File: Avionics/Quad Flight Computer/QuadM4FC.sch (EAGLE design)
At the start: 1 part, among them U1 INF-PG-LQFP-100-11-7000X7000E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

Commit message: Added avionics library as Eagle-Library submodule.
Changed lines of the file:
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@@
+</nets>
+</sheet>
+<sheet>
+<description>Sensors</description>
+<plain>
+</plain>
+<instances>
+</instances>
+<busses>
+</busses>
+<nets>
+</nets>
+</sheet>
+<sheet>
+<description>2.4 GHz Radio</description>
+<plain>
+</plain>
+<instances>
+</instances>
+<busses>
+</busses>
+<nets>
+</nets>
+</sheet>
+<sheet>
+<description>900MHz Radio</description>
+<plain>
+</plain>
+<instances>
+</instances>
+<busses>
+</busses>
+<nets>
+</nets>
+</sheet>
+<sheet>
+<description>Flash Memory</description>
+<plain>
+</plain>
+<instances>
+</instances>
+<busses>
+</busses>
+<nets>
+</nets>
+</sheet>
+<sheet>
+<description>Power</description>
+<plain>
+</plain>
+<instances>
+</instances>
+<busses>
+</busses>
+<nets>
+</nets>
+</sheet>
+<sheet>
+<description>Connectors</description>
+<plain>
+</plain>
+<instances>
+</instances>
+<busses>
+</busses>
+<nets>
 </nets>
 </sheet>

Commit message: Added IMU to library
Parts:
- added U2: MPU-9250, Invesense:MPU-9250
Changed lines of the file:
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@@
 <layers>
 <layer number="1" name="Top" color="4" fill="1" visible="no" active="no"/>
+<layer number="2" name="Route2" color="1" fill="3" visible="no" active="no"/>
+<layer number="3" name="Route3" color="4" fill="3" visible="no" active="no"/>
+<layer number="14" name="Route14" color="1" fill="6" visible="no" active="no"/>
+<layer number="15" name="Route15" color="4" fill="6" visible="no" active="no"/>
 <layer number="16" name="Bottom" color="1" fill="1" visible="no" active="no"/>
 <layer number="17" name="Pads" color="2" fill="1" visible="no" active="no"/>
@@
 <layer number="48" name="Document" color="7" fill="1" visible="no" active="no"/>
 <layer number="49" name="Reference" color="7" fill="1" visible="no" active="no"/>
+<layer number="50" name="dxf" color="7" fill="1" visible="no" active="no"/>
 <layer number="51" name="tDocu" color="7" fill="1" visible="no" active="no"/>
 <layer number="52" name="bDocu" color="7" fill="1" visible="no" active="no"/>
+<layer number="53" name="tGND_GNDA" color="7" fill="1" visible="no" active="no"/>
+<layer number="54" name="bGND_GNDA" color="7" fill="1" visible="no" active="no"/>
+<layer number="56" name="wert" color="7" fill="1" visible="no" active="no"/>
 <layer number="91" name="Nets" color="2" fill="1" visible="yes" active="yes"/>
 <layer number="92" name="Busses" color="1" fill="1" visible="yes" active="yes"/>
@@
 <layer number="97" name="Info" color="7" fill="1" visible="yes" active="yes"/>
 <layer number="98" name="Guide" color="6" fill="1" visible="yes" active="yes"/>
+<layer number="100" name="Muster" color="7" fill="1" visible="yes" active="yes"/>
+<layer number="101" name="Patch_Top" color="7" fill="1" visible="yes" active="yes"/>
+<layer number="102" name="Vscore" color="7" fill="1" visible="yes" active="yes"/>
+<layer number="103" name="tMap" color="7" fill="1" visible="yes" active="yes"/>
+<layer number="104" name="Name" color="7" fill="1" visible="yes" active="yes"/>
+<layer number="105" name="tPlate" color="7" fill="1" visible="yes" active="yes"/>
+<layer number="106" name="bPlate" color="7" fill="1" visible="yes" active="yes"/>
+<layer number="107" name="Crop" color="7" fill="1" visible="yes" active="yes"/>
+<layer number="108" name="fp8" color="7" fill="1" visible="yes" active="yes"/>
+<layer number="109" name="fp9" color="7" fill="1" visible="yes" active="yes"/>
+<layer number="110" name="fp0" color="7" fill="1" visible="yes" active="yes"/>
+<layer number="116" name="Patch_BOT" color="7" fill="1" visible="yes" active="yes"/>
+<layer number="121" name="_tsilk" color="7" fill="1" visible="yes" active="yes"/>
+<layer number="122" name="_bsilk" color="7" fill="1" visible="yes" active="yes"/>
+<layer number="123" name="tTestmark" color="7" fill="1" visible="yes" active="yes"/>
+<layer number="124" name="bTestmark" color="7" fill="1" visible="yes" active="yes"/>
+<layer number="125" name="_tNames" color="7" fill="1" visible="yes" active="yes"/>
+<layer number="131" name="tAdjust" color="7" fill="1" visible="yes" active="yes"/>
+<layer number="132" name="bAdjust" color="7" fill="1" visible="yes" active="yes"/>
+<layer number="144" name="Drill_legend" color="7" fill="1" visible="yes" active="yes"/>
+<layer number="151" name="HeatSink" color="7" fill="1" visible="yes" active="yes"/>
+<layer number="199" name="Contour" color="7" fill="1" visible="yes" active="yes"/>
+<layer number="200" name="200bmp" color="7" fill="1" visible="yes" active="yes"/>
+<layer number="201" name="201bmp" color="7" fill="1" visible="yes" active="yes"/>
+<layer number="202" name="202bmp" color="7" fill="1" visible="yes" active="yes"/>
+<layer number="203" name="203bmp" color="7" fill="1" visible="yes" active="yes"/>
+<layer number="204" name="204bmp" color="7" fill="1" visible="yes" active="yes"/>
+<layer number="205" name="205bmp" color="7" fill="1" visible="yes" active="yes"/>
+<layer number="206" name="206bmp" color="7" fill="1" visible="yes" active="yes"/>
+<layer number="207" name="207bmp" color="7" fill="1" visible="yes" active="yes"/>
+<layer number="208" name="208bmp" color="7" fill="1" visible="yes" active="yes"/>
+<layer number="209" name="209bmp" color="7" fill="1" visible="yes" active="yes"/>
+<layer number="210" name="210bmp" color="7" fill="1" visible="yes" active="yes"/>
+<layer number="211" name="211bmp" color="7" fill="1" visible="yes" active="yes"/>
+<layer number="212" name="212bmp" color="7" fill="1" visible="yes" active="yes"/>
+<layer number="213" name="213bmp" color="7" fill="1" visible="yes" active="yes"/>
+<layer number="214" name="214bmp" color="7" fill="1" visible="yes" active="yes"/>
+<layer number="215" name="215bmp" color="7" fill="1" visible="yes" active="yes"/>
+<layer number="216" name="216bmp" color="7" fill="1" visible="yes" active="yes"/>
+<layer number="217" name="217bmp" color="7" fill="1" visible="yes" active="yes"/>
+<layer number="218" name="218bmp" color="7" fill="1" visible="yes" active="yes"/>
+<layer number="219" name="219bmp" color="7" fill="1" visible="yes" active="yes"/>
+<layer number="220" name="220bmp" color="7" fill="1" visible="yes" active="yes"/>
+<layer number="221" name="221bmp" color="7" fill="1" visible="yes" active="yes"/>
+<layer number="222" name="222bmp" color="7" fill="1" visible="yes" active="yes"/>
+<layer number="223" name="223bmp" color="7" fill="1" visible="yes" active="yes"/>
+<layer number="224" name="224bmp" color="7" fill="1" visible="yes" active="yes"/>
+<layer number="250" name="Descript" color="7" fill="1" visible="yes" active="yes"/>
+<layer number="251" name="SMDround" color="7" fill="1" visible="yes" active="yes"/>
+<layer number="254" name="cooling" color="7" fill="1" visible="yes" active="yes"/>
 </layers>
 <schematic xreflabel="%F%N/%S.%C%R" xrefpart="/%S.%C%R">
@@
 <parts>
 <part name="U1" library="XMC4500-F100K1024 AB" deviceset="INF-PG-LQFP-100-11-7000X7000E9" device="LQFP-100"/>
+<part name="U2" library="Invesense" deviceset="MPU-9250" device=""/>
 </parts>
 <sheets>
@@
 </plain>
 <instances>
+<instance part="U2" gate="G$1" x="0" y="0"/>
 </instances>
 <busses>

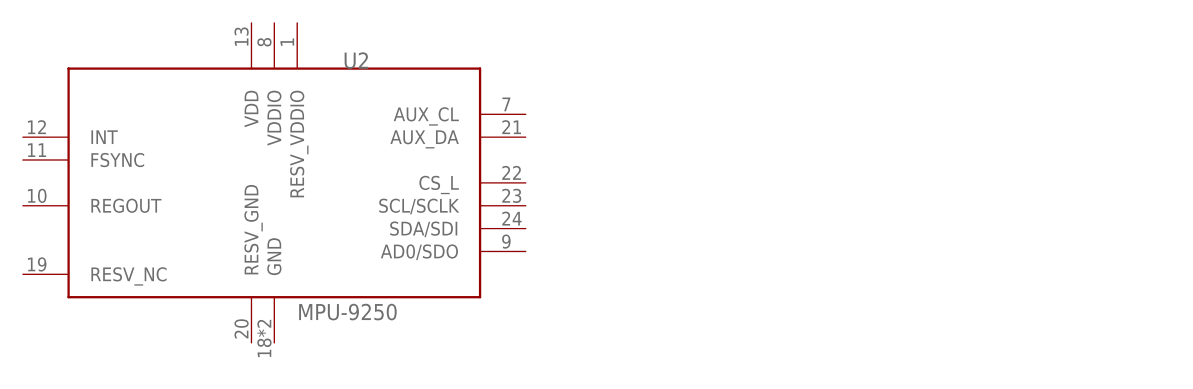
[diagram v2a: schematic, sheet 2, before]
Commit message: Added barometer
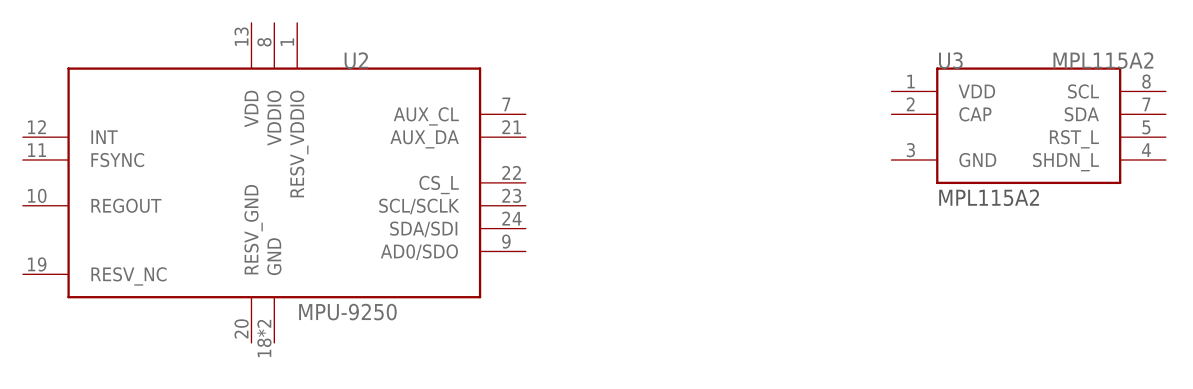
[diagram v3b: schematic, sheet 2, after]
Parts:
- added U3: MPL115A2, Sensors:MPL115A2
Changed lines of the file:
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@@
 <part name="U1" library="XMC4500-F100K1024 AB" deviceset="INF-PG-LQFP-100-11-7000X7000E9" device="LQFP-100"/>
 <part name="U2" library="Invesense" deviceset="MPU-9250" device=""/>
+<part name="U3" library="Sensors" deviceset="MPL115A2" device=""/>
 </parts>
 <sheets>
@@
 <instances>
 <instance part="U2" gate="G$1" x="0" y="0"/>
+<instance part="U3" gate="G$1" x="83.82" y="5.08"/>
 </instances>
 <busses>

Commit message: Added memory module
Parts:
- added U4: S25FL127S, memory:S25FL127S
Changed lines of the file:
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@@
 <part name="U2" library="Invesense" deviceset="MPU-9250" device=""/>
 <part name="U3" library="Sensors" deviceset="MPL115A2" device=""/>
+<part name="U4" library="memory" deviceset="S25FL127S" device=""/>
 </parts>
 <sheets>
@@
 </plain>
 <instances>
+<instance part="U4" gate="G$1" x="0" y="0"/>
 </instances>
 <busses>

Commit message: Added radio part
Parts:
- added U5: CC2520, ti_rf:CC2520
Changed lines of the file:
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@@
 <part name="U3" library="Sensors" deviceset="MPL115A2" device=""/>
 <part name="U4" library="memory" deviceset="S25FL127S" device=""/>
+<part name="U5" library="ti_rf" deviceset="CC2520" device=""/>
 </parts>
 <sheets>
@@
 </plain>
 <instances>
+<instance part="U5" gate="G$1" x="0" y="0"/>
 </instances>
 <busses>

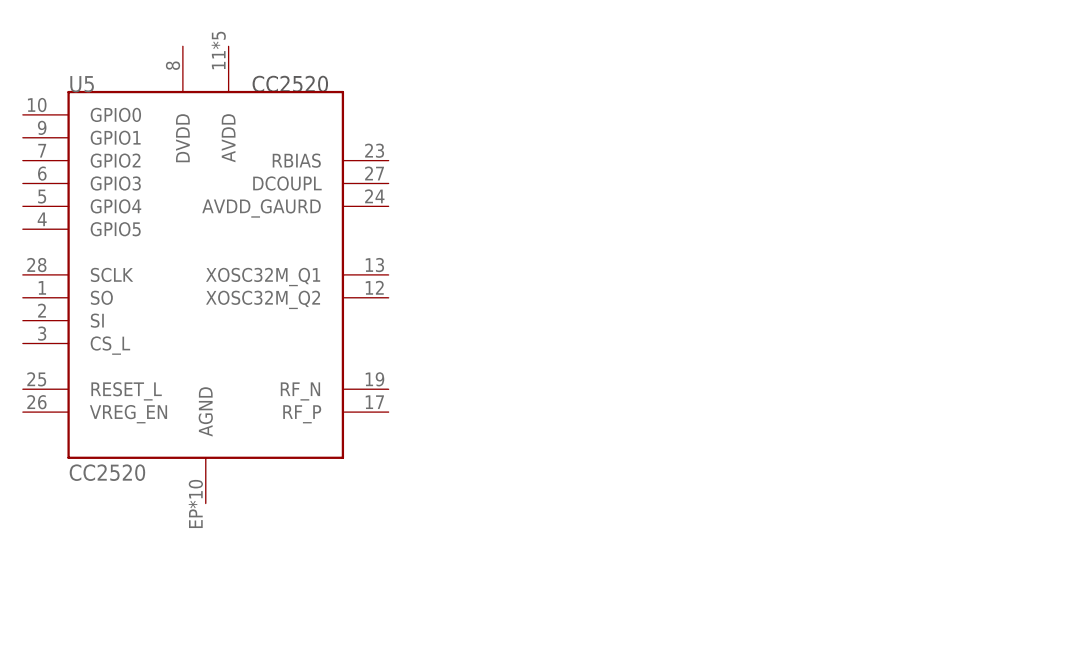
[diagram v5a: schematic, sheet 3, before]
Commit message: Added radio components
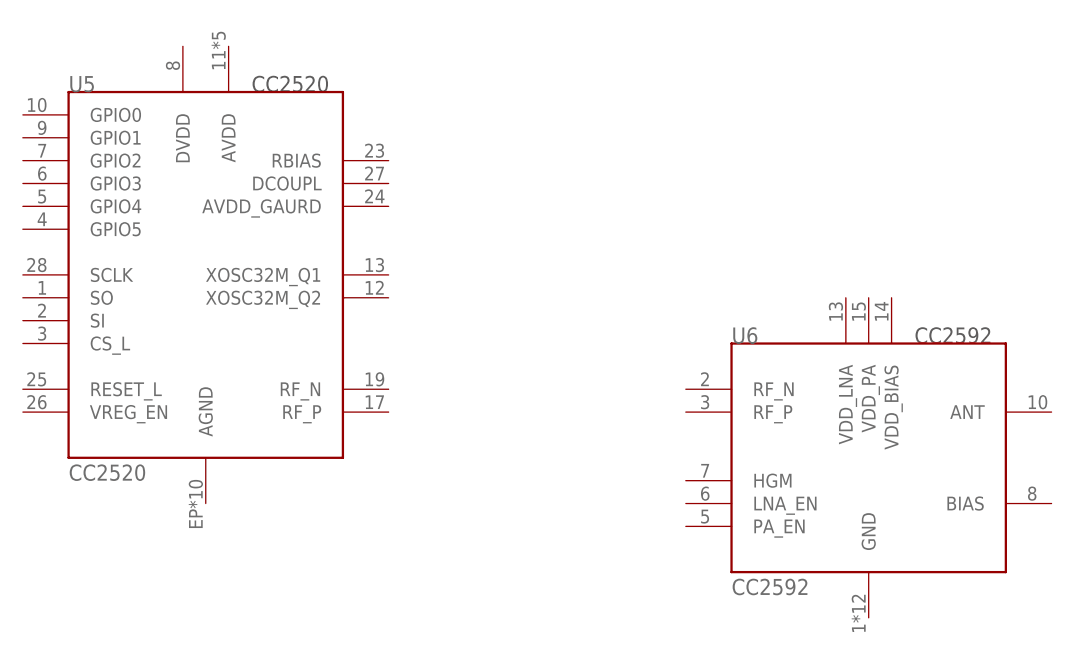
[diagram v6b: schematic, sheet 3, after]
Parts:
- added U6: CC2592, ti_rf:CC2592
- added U7: CC1120, ti_rf:CC1120
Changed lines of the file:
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@@
 <part name="U4" library="memory" deviceset="S25FL127S" device=""/>
 <part name="U5" library="ti_rf" deviceset="CC2520" device=""/>
+<part name="U6" library="ti_rf" deviceset="CC2592" device=""/>
+<part name="U7" library="ti_rf" deviceset="CC1120" device=""/>
 </parts>
 <sheets>
@@
 <instances>
 <instance part="U5" gate="G$1" x="0" y="0"/>
+<instance part="U6" gate="G$1" x="73.66" y="-22.86"/>
 </instances>
 <busses>
@@
 </plain>
 <instances>
+<instance part="U7" gate="G$1" x="0" y="0"/>
 </instances>
 <busses>

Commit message: Added RF base station project
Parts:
- added U8: CC1190, ti_rf:CC1190
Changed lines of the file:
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@@
 <part name="U6" library="ti_rf" deviceset="CC2592" device=""/>
 <part name="U7" library="ti_rf" deviceset="CC1120" device=""/>
+<part name="U8" library="ti_rf" deviceset="CC1190" device=""/>
 </parts>
 <sheets>
@@
 <instances>
 <instance part="U7" gate="G$1" x="0" y="0"/>
+<instance part="U8" gate="G$1" x="93.98" y="-10.16"/>
 </instances>
 <busses>
